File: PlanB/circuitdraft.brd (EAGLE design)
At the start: 55 x 62 mm, 17 parts, among them Q1 16 MHz

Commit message: ud
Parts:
- moved REG 1.00 mm to (45.0, 42.0)
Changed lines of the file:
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@@
 <attribute name="VALUE" x="46.225" y="25.725" size="1.27" layer="27" rot="R180"/>
 </element>
-<element name="REG" library="pinhead" library_urn="urn:adsk.eagle:library:325" package="1X04" package3d_urn="urn:adsk.eagle:package:22407/2" value="" x="46" y="42" smashed="yes" rot="R270">
-<attribute name="NAME" x="47.8288" y="47.1562" size="1.27" layer="25" ratio="10" rot="R270"/>
-<attribute name="POPULARITY" value="91" x="15.52" y="8.98" size="1.778" layer="27" rot="R270" display="off"/>
-<attribute name="VALUE" x="42.825" y="47.08" size="1.27" layer="27" rot="R270"/>
+<element name="REG" library="pinhead" library_urn="urn:adsk.eagle:library:325" package="1X04" package3d_urn="urn:adsk.eagle:package:22407/2" value="" x="45" y="42" smashed="yes" rot="R270">
+<attribute name="NAME" x="46.8288" y="47.1562" size="1.27" layer="25" ratio="10" rot="R270"/>
+<attribute name="POPULARITY" value="91" x="14.52" y="8.98" size="1.778" layer="27" rot="R270" display="off"/>
+<attribute name="VALUE" x="41.825" y="47.08" size="1.27" layer="27" rot="R270"/>
 </element>
 <element name="SERVO" library="pinhead" library_urn="urn:adsk.eagle:library:325" package="1X05" package3d_urn="urn:adsk.eagle:package:22469/2" value="" x="73.48" y="33.32" smashed="yes" rot="R270">
@@
 <wire x1="49.87" y1="40.25" x2="52.41" y2="40.25" width="0" layer="19" extent="1-1"/>
 <wire x1="49.87" y1="37.71" x2="52.41" y2="37.71" width="0" layer="19" extent="1-1"/>
-<wire x1="46" y1="45.81" x2="49.87" y2="45.33" width="0" layer="19" extent="1-1"/>
+<wire x1="45" y1="45.81" x2="49.87" y2="45.33" width="0" layer="19" extent="1-1"/>
 </signal>
 <signal name="SIGNAL1">

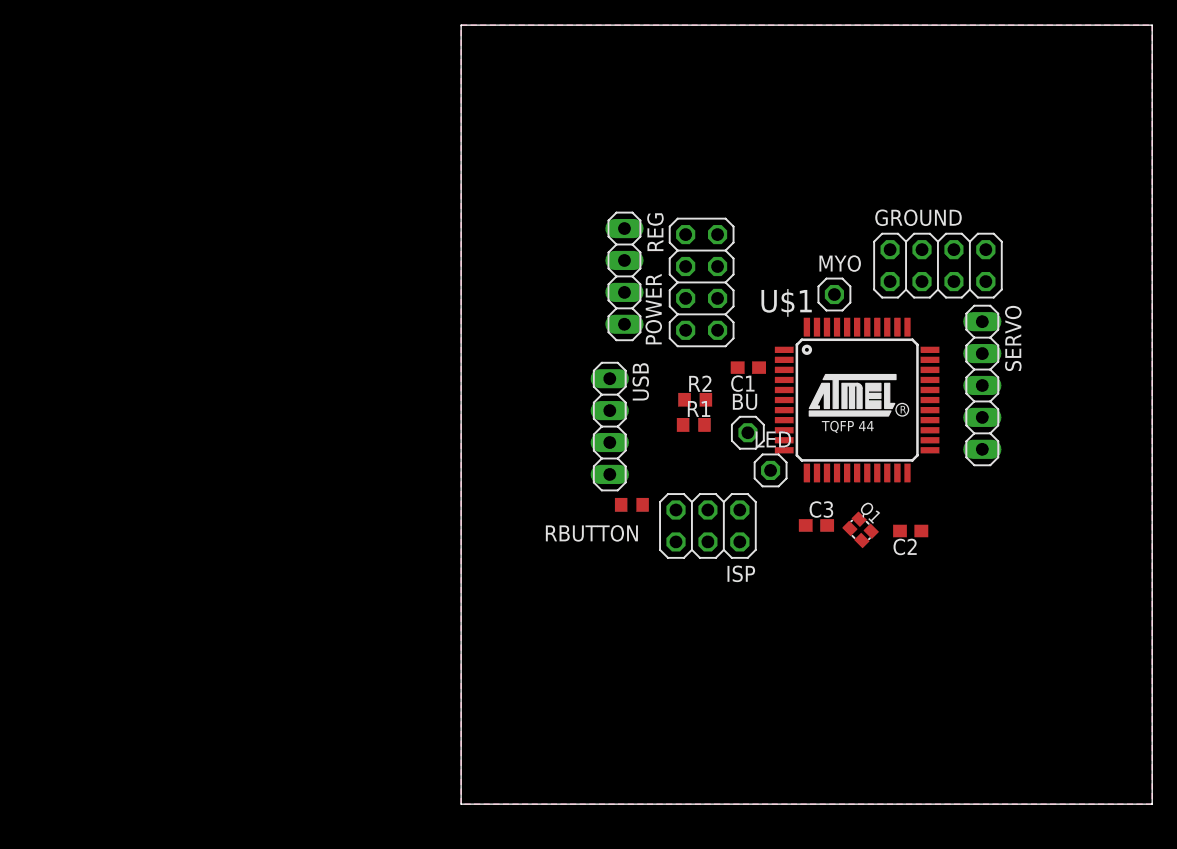
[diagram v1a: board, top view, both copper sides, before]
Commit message: using external board for charging, removes regulator, needs tweaking
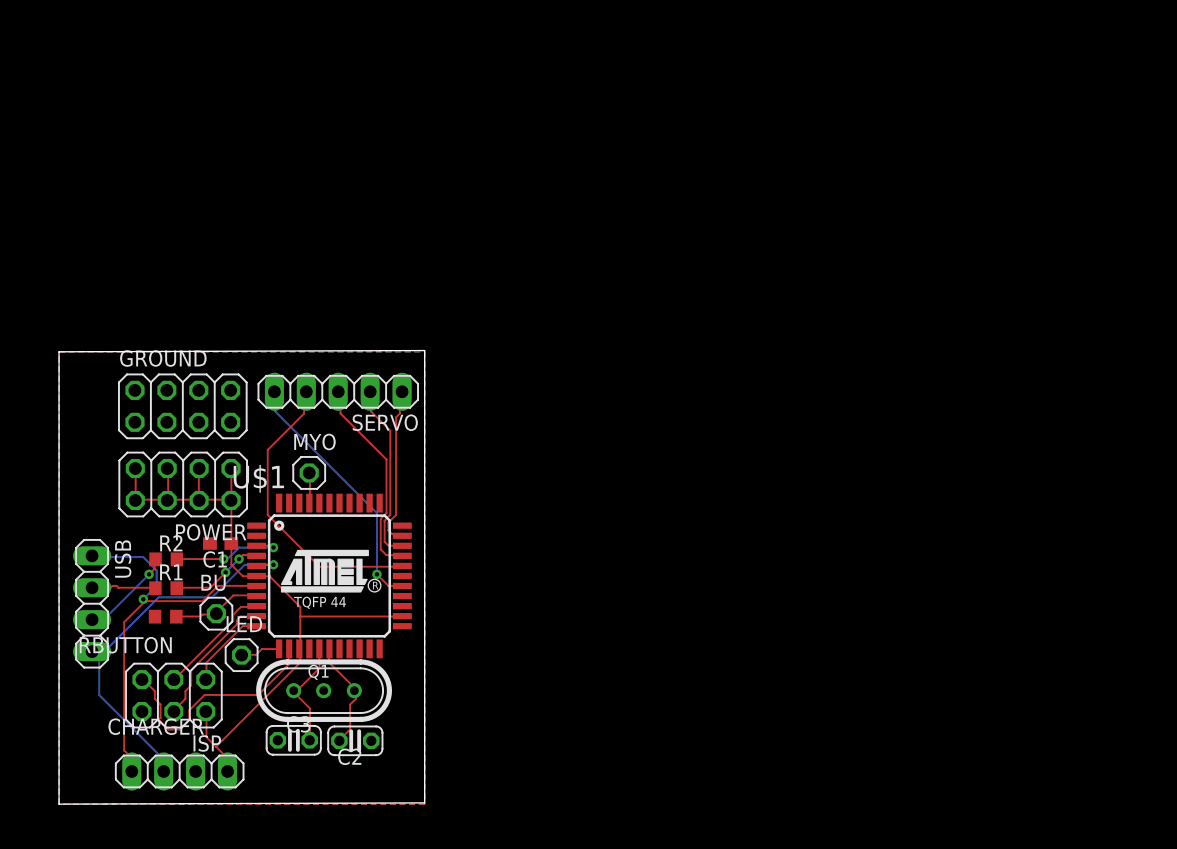
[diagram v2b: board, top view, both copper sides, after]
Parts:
- removed REG: (no value), pinhead:1X04
- added CHARGER: (no value), pinhead:1X04
- C2, C3: device rcl:C0603 -> rcl:C025-024X044
- Q1: device crystal-geyer_V1_0:2.0X1.6_KX-5 -> crystal:HC49U
- moved GROUND 61.1 mm to (9.85, 31.7)
- moved SERVO 51.3 mm to (22.2, 32.8), turned to 180 degrees
- moved C2 47.2 mm to (23.6, 5.04)
- moved C3 45.0 mm to (18.7, 5.08)
- moved BU 44.7 mm to (12.5, 15.2)
- moved ISP 44.6 mm to (9.14, 8.64)
- moved LED 44.6 mm to (14.5, 11.9)
- moved Q1 44.6 mm to (21.1, 9.03), turned to 0 degrees
- moved POWER 44.3 mm to (9.88, 25.4), turned to 180 degrees
- moved C1 44.3 mm to (12.9, 20.7)
- moved U$1 44.3 mm to (21.5, 18.2)
- moved MYO 44.1 mm to (19.9, 26.4)
- moved R2 44.0 mm to (8.53, 19.5)
- moved R1 44.0 mm to (8.52, 17.2)
- moved USB 43.5 mm to (2.63, 15.9)
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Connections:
- removed net B+: REG.3
- removed net ENABLE: REG.4
- removed net N$8: C1.1, U$1.6
- net GND: now also CHARGER.3; no longer REG.2
- net POWER: now also C1.1, CHARGER.4, U$1.6; no longer REG.1, U$1.2
- net UGND: now also CHARGER.2
- net VBUS: now also CHARGER.1
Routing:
- net POWER: track 0.00 -> 57.4 mm
- net VBUS: track 0.00 -> 32.4 mm, vias 0 -> 1
- net UGND: track 0.00 -> 30.9 mm, vias 0 -> 1
- net SIGNAL1: track 0.00 -> 23.5 mm
- net SIGNAL5: track 0.00 -> 20.3 mm, vias 0 -> 1
- net RST: track 0.00 -> 18.5 mm
- net SIGNAL2: track 0.00 -> 16.3 mm
- net SIGNAL4: track 0.00 -> 14.3 mm
- net SIGNAL3: track 0.00 -> 12.8 mm
- net MOSI: track 0.00 -> 11.0 mm
- net N$2: track 0.00 -> 9.49 mm, vias 0 -> 2
- net SCK: track 0.00 -> 9.29 mm
- net N$5: track 0.00 -> 8.92 mm
- net N$6: track 0.00 -> 8.89 mm
- net N$4: track 0.00 -> 7.47 mm, vias 0 -> 2
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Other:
- board size 55 x 62 mm -> 29.1 x 36.1 mm

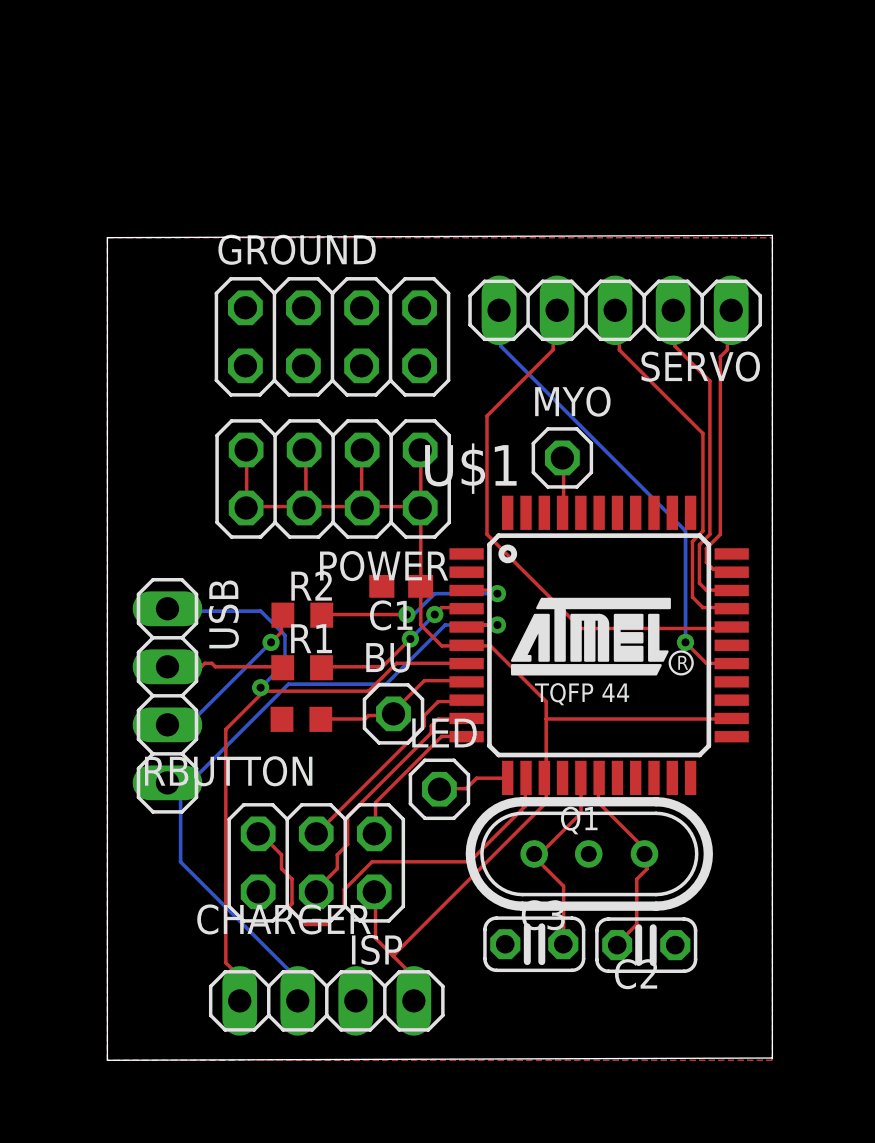
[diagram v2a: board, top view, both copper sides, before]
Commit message: added regulator
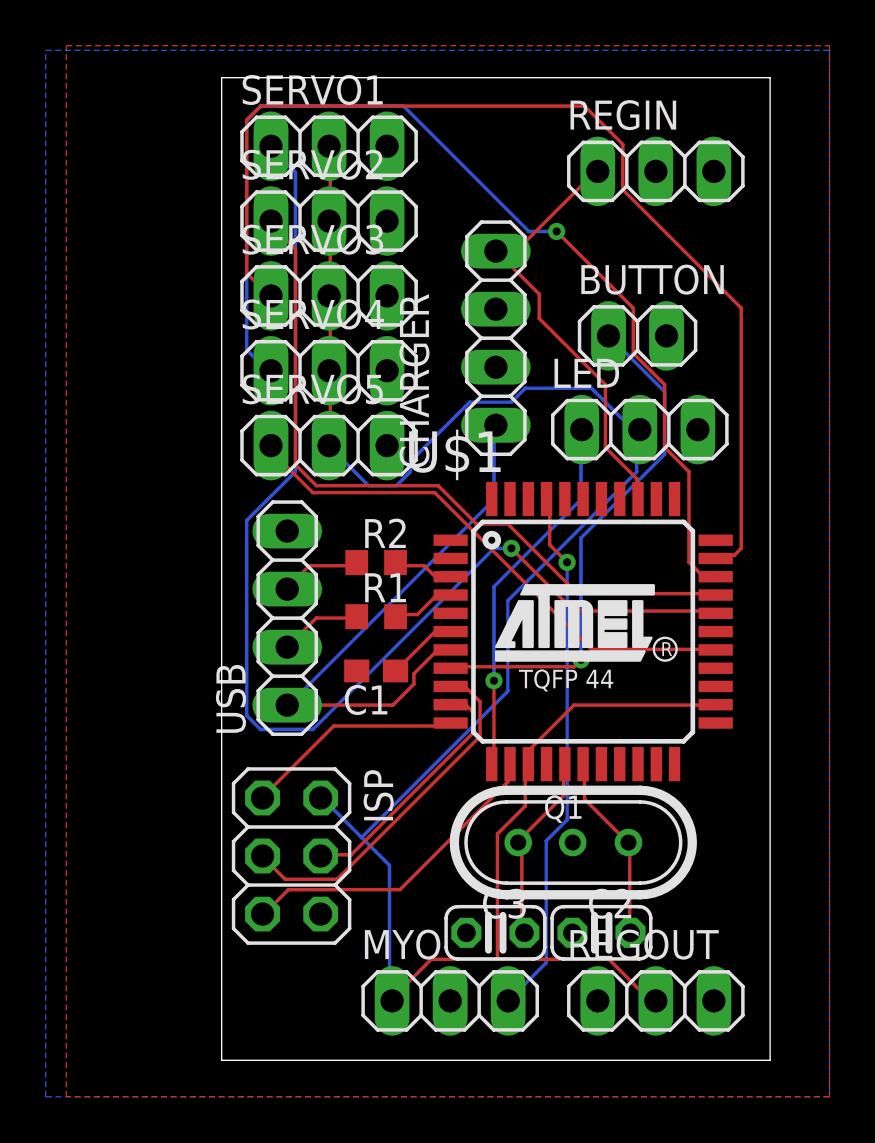
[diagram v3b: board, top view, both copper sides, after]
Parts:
- removed BU: (no value), pinhead:1X01
- removed GROUND, POWER: (no value), pinhead:2X04
- removed RBUTTON: 220 Ohm, rcl:R0603
- removed SERVO: (no value), pinhead:1X05
- added BUTTON: (no value), pinhead:1X02
- added REGIN, REGOUT, SERVO1, SERVO2, SERVO3, SERVO4, SERVO5: (no value), pinhead:1X03
- LED, MYO: device pinhead:1X01 -> pinhead:1X03
- moved CHARGER 29.9 mm to (17.0, 31.6), turned to 90 degrees
- moved MYO 24.3 mm to (15.0, 2.60)
- moved LED 18.0 mm to (23.3, 27.6)
- moved USB 6.25 mm to (7.87, 19.4), turned to 90 degrees
- moved R2 3.97 mm to (11.8, 21.8)
- moved R1 3.93 mm to (11.8, 19.4)
- moved C1 3.86 mm to (11.8, 17.0)
- moved C2 2.03 mm to (21.6, 5.58), turned to 0 degrees
- moved C3 1.77 mm to (17.0, 5.58)
- moved ISP 1.12 mm to (8.06, 8.94), turned to 270 degrees
- moved U$1 0.92 mm to (20.8, 18.8)
- moved Q1 0.86 mm to (20.4, 9.53)
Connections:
- removed net MIDDLE: U$1.36
- removed net MYOSIGNAL: MYO.1, U$1.41
- removed net UGND: CHARGER.2, U$1.5, USB.4
- new net N$1: MYO.3, U$1.41
- new net N$3: C1.1, U$1.6
- new net VBAT: CHARGER.4, REGIN.1, U$1.36
- net GND: now also BUTTON.2, CHARGER.2, LED.3, MYO.2, REGIN.2, REGOUT.3, SERVO1.3, SERVO2.3, SERVO3.3, SERVO4.3, SERVO5.3, U$1.5, USB.4; no longer GROUND.1, GROUND.2, GROUND.3, GROUND.4, GROUND.5, GROUND.6, GROUND.7, GROUND.8, RBUTTON.2
- net INTERRUPT: now also BUTTON.1; no longer BU.1, RBUTTON.1
- net POWER: now also LED.2, MYO.1, REGOUT.2, SERVO1.2, SERVO2.2, SERVO3.2, SERVO4.2, SERVO5.2; no longer C1.1, CHARGER.4, POWER.1, POWER.2, POWER.3, POWER.4, POWER.5, POWER.6, POWER.7, POWER.8, U$1.6
- net SIGNAL1: now also SERVO1.1; no longer SERVO.4
- net SIGNAL2: now also SERVO2.1; no longer SERVO.3
- net SIGNAL3: now also SERVO3.1; no longer SERVO.1
- net SIGNAL4: now also SERVO4.1; no longer SERVO.2
- net SIGNAL5: now also SERVO5.1; no longer SERVO.5
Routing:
- net POWER: track 57.4 -> 95.5 mm
- net SIGNAL3: track 12.8 -> 46.7 mm
- net SIGNAL4: track 14.3 -> 45.9 mm, vias 0 -> 1
- net UGND: track 30.9 -> 0.00 mm, vias 1 -> 0
- net SIGNAL1: track 23.5 -> 51.5 mm, vias 0 -> 1
- net N$1: track 0.00 -> 23.5 mm, vias 0 -> 1
- net VBAT: track 0.00 -> 19.6 mm
- net SIGNAL2: track 16.3 -> 31.8 mm
- net INTERRUPT: track 7.21 -> 22.6 mm, vias 0 -> 1
- net DATAIN: track 3.18 -> 16.3 mm, vias 0 -> 1
- net VBUS: track 32.4 -> 24.5 mm, vias 1 -> 0
- net N$2: track 9.49 -> 2.71 mm, vias 2 -> 0
- net SCK: track 9.29 -> 15.6 mm
- net N$4: track 7.47 -> 2.83 mm, vias 2 -> 0
- net RST: track 18.5 -> 14.0 mm
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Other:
- board size 29.1 x 36.1 mm -> 24 x 43 mm

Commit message: ajusted to thorugh whole parts
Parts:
- C1: device rcl:C0603 -> rcl:C025-024X044
- R1, R2: device rcl:R0603 -> rcl:0204/7
- moved C2 5.74 mm to (26.8, 8.02), turned to 90 degrees
- moved MYO 5.60 mm to (9.40, 2.60)
- moved C1 5.09 mm to (13.5, 12.2)
- moved C3 4.89 mm to (12.7, 7.98), turned to 90 degrees
- moved R2 3.36 mm to (10.5, 18.7), turned to 90 degrees
- moved Q1 1.71 mm to (19.8, 7.93)
- moved R1 1.36 mm to (12.9, 18.7), turned to 90 degrees
- moved USB 0.30 mm to (7.57, 19.4)
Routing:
- net DATAIN: track 16.3 -> 79.6 mm, vias 1 -> 0
- net VBUS: track 24.5 -> 46.5 mm
- net SIGNAL4: track 45.9 -> 25.0 mm, vias 1 -> 0
- net SIGNAL3: track 46.7 -> 27.9 mm, vias 0 -> 1
- net POWER: track 95.5 -> 108.7 mm, vias 0 -> 1
- net SIGNAL1: track 51.5 -> 39.2 mm
- net INTERRUPT: track 22.6 -> 30.8 mm
- net N$1: track 23.5 -> 30.6 mm, vias 1 -> 2
- net N$3: track 3.12 -> 8.59 mm, vias 0 -> 1
- net N$2: track 2.71 -> 6.57 mm
- net D-: track 3.56 -> 6.99 mm
- net D+: track 3.58 -> 6.68 mm
- net N$5: track 8.38 -> 11.4 mm
- net N$6: track 8.26 -> 10.8 mm
- net SIGNAL2: track 31.8 -> 34.2 mm, vias 0 -> 1
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
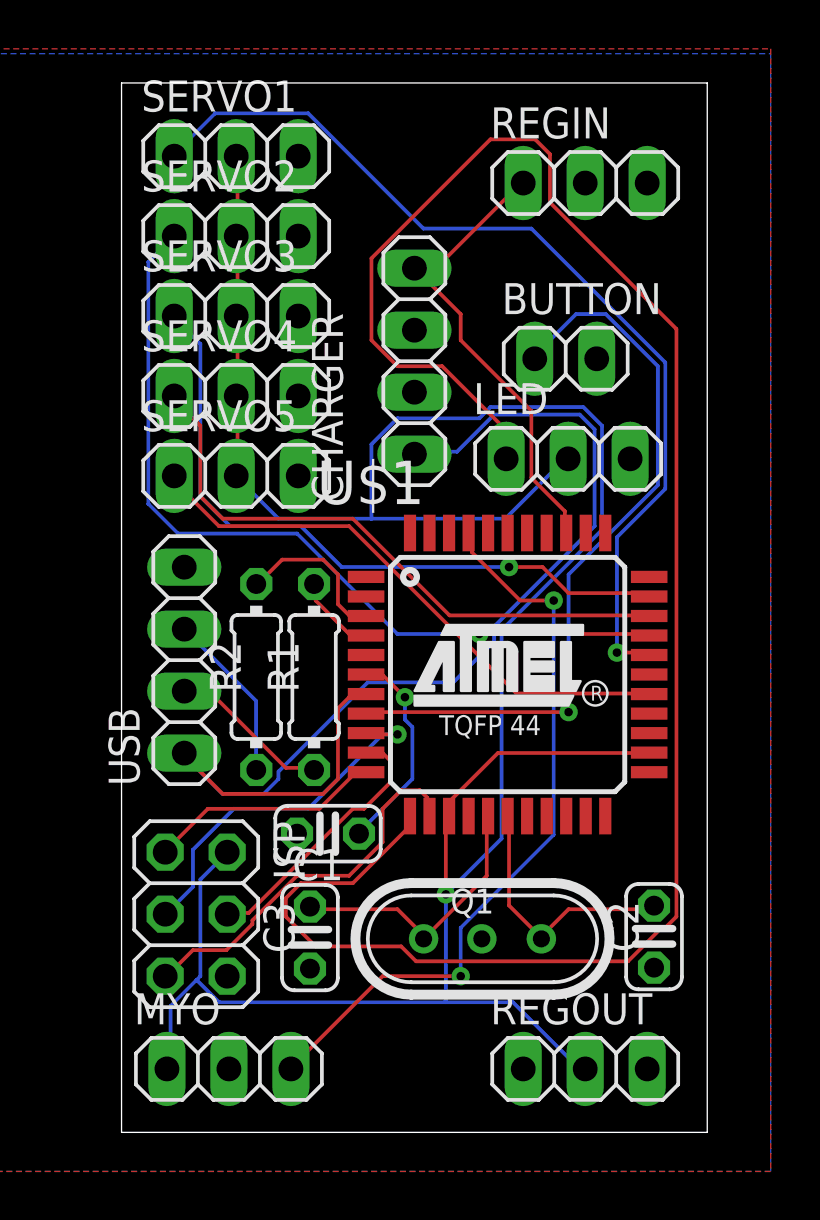
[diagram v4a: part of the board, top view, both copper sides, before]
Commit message: fixed orientation of regulator connections
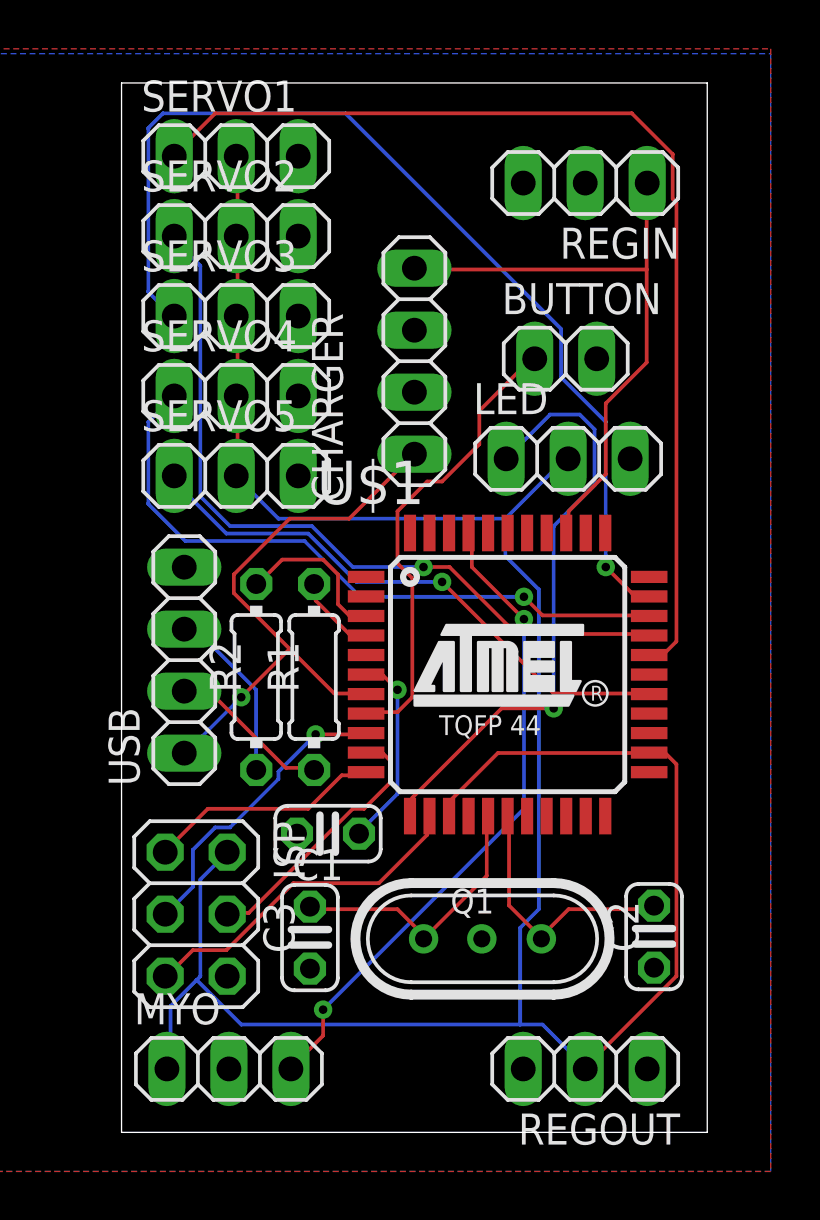
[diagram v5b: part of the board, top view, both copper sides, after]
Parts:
- turned REGIN to 180 degrees
- turned REGOUT to 180 degrees
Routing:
- net DATAIN: track 79.6 -> 24.8 mm, vias 0 -> 1
- net VBUS: track 46.5 -> 23.4 mm, vias 0 -> 1
- net SIGNAL3: track 27.9 -> 41.8 mm
- net INTERRUPT: track 30.8 -> 19.1 mm, vias 1 -> 0
- net POWER: track 108.7 -> 102.5 mm, vias 1 -> 0
- net VBAT: track 19.6 -> 25.2 mm
- net SIGNAL1: track 39.2 -> 43.3 mm, vias 1 -> 0
- net N$1: track 30.6 -> 26.9 mm
- net SCK: track 14.8 -> 12.4 mm
- net SIGNAL2: track 34.2 -> 31.8 mm
- net SIGNAL4: track 25.0 -> 27.3 mm, vias 0 -> 1
- net RST: track 15.7 -> 14.0 mm
- net N$3: track 8.59 -> 8.08 mm
- net SIGNAL5: vias 0 -> 1
